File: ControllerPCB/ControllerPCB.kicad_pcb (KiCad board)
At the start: 2 copper layers, 48 parts, among them U2 STM32F439ZITx, Y2 WE-XTAL_CFPX-218

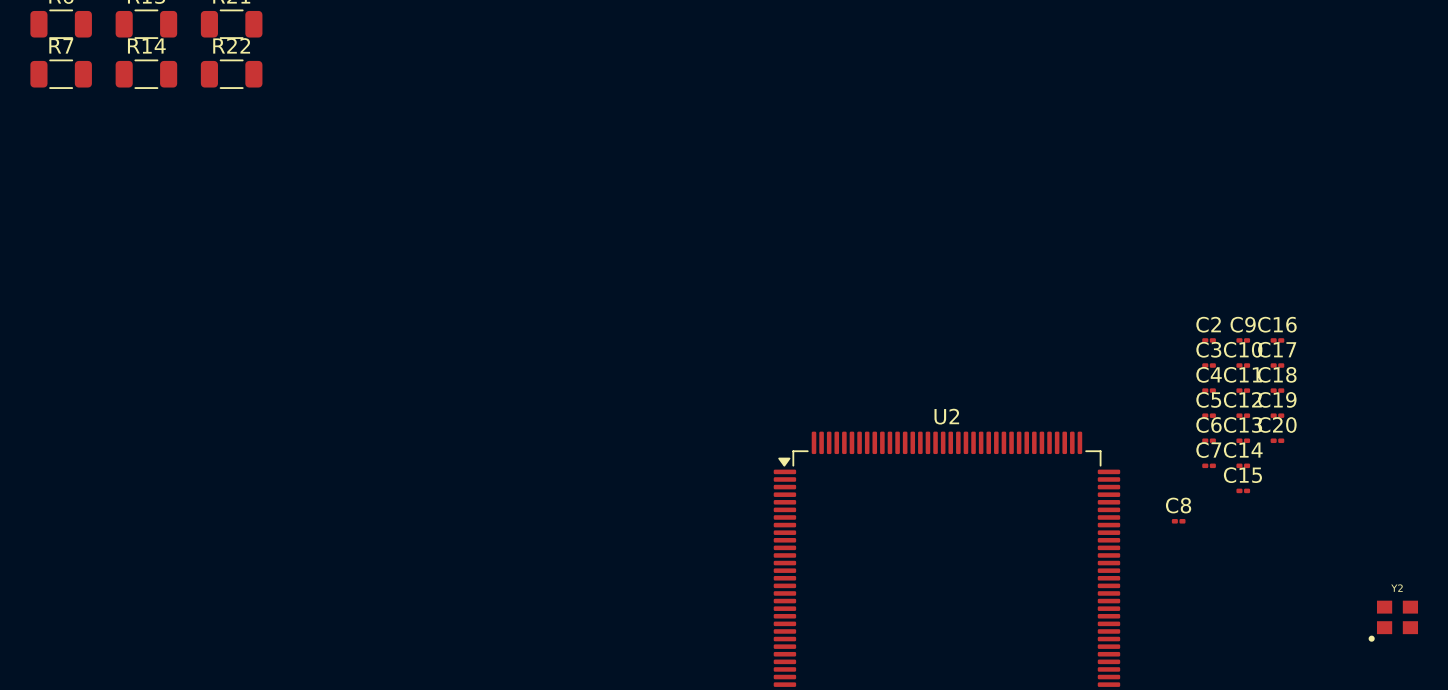
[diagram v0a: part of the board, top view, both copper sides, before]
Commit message: Added footprints to the resistors and capacitors and values of Crystall Oscillator capacitors.
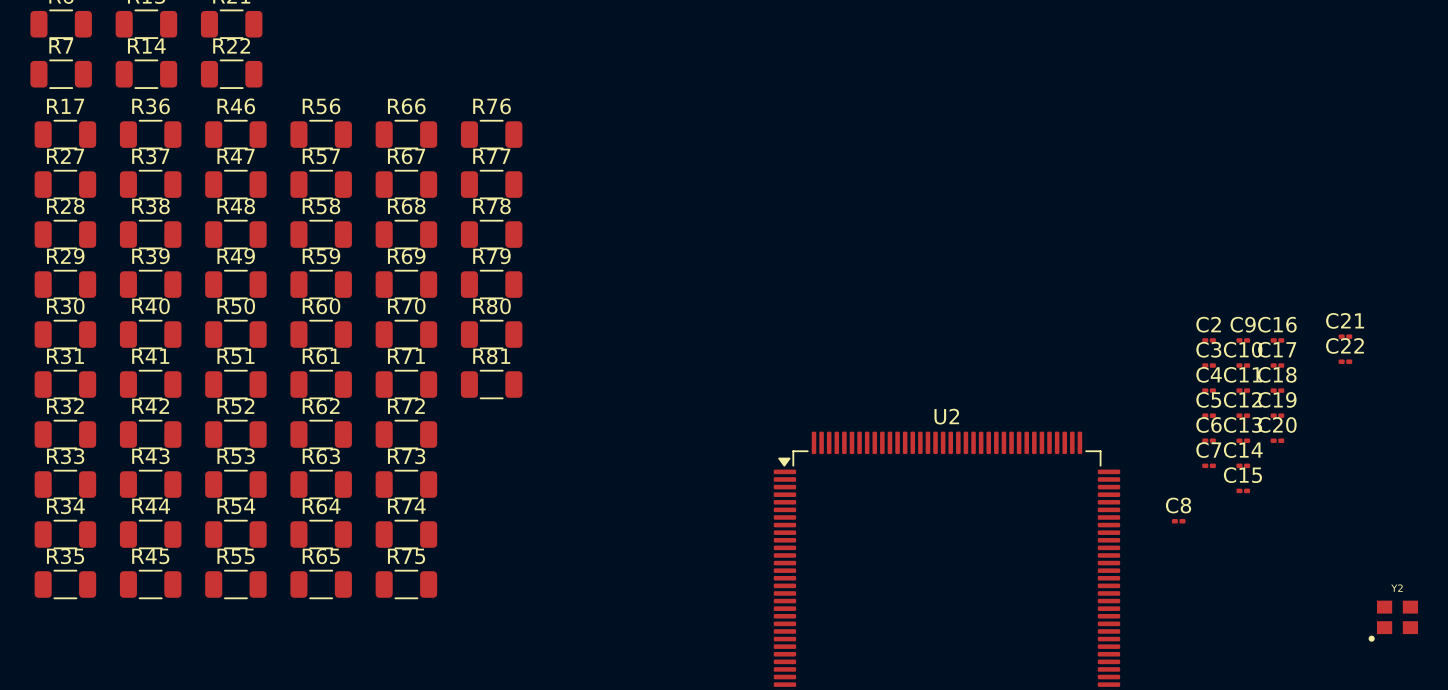
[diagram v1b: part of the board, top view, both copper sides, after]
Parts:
- added C21: 10p, Capacitor_SMD:C_01005_0402Metric, F.Cu at (170.7, 78.3)
- added C22: 10p, Capacitor_SMD:C_01005_0402Metric, F.Cu at (170.7, 80.0)
- added R17: 10k, Resistor_SMD:R_1206_3216Metric, F.Cu at (86.5, 65.0)
- added R27: 10k, Resistor_SMD:R_1206_3216Metric, F.Cu at (86.5, 68.3)
- added R28: 10k, Resistor_SMD:R_1206_3216Metric, F.Cu at (86.5, 71.6)
- added R29: 10k, Resistor_SMD:R_1206_3216Metric, F.Cu at (86.5, 74.9)
- added R30: 10k, Resistor_SMD:R_1206_3216Metric, F.Cu at (86.5, 78.2)
- added R31: 10k, Resistor_SMD:R_1206_3216Metric, F.Cu at (86.5, 81.5)
- added R32: 10k, Resistor_SMD:R_1206_3216Metric, F.Cu at (86.5, 84.8)
- added R33: 10k, Resistor_SMD:R_1206_3216Metric, F.Cu at (86.5, 88.1)
- added R34: 10k, Resistor_SMD:R_1206_3216Metric, F.Cu at (86.5, 91.4)
- added R35: 10k, Resistor_SMD:R_1206_3216Metric, F.Cu at (86.5, 94.7)
- added R36: 10k, Resistor_SMD:R_1206_3216Metric, F.Cu at (92.1, 65.0)
- added R37: 10k, Resistor_SMD:R_1206_3216Metric, F.Cu at (92.1, 68.3)
- added R38: 10k, Resistor_SMD:R_1206_3216Metric, F.Cu at (92.1, 71.6)
- added R39: 10k, Resistor_SMD:R_1206_3216Metric, F.Cu at (92.1, 74.9)
- added R40: 10k, Resistor_SMD:R_1206_3216Metric, F.Cu at (92.1, 78.2)
- added R41: 10k, Resistor_SMD:R_1206_3216Metric, F.Cu at (92.1, 81.5)
- added R42: 10k, Resistor_SMD:R_1206_3216Metric, F.Cu at (92.1, 84.8)
- added R43: 10k, Resistor_SMD:R_1206_3216Metric, F.Cu at (92.1, 88.1)
- added R44: 10k, Resistor_SMD:R_1206_3216Metric, F.Cu at (92.1, 91.4)
- added R45: 10k, Resistor_SMD:R_1206_3216Metric, F.Cu at (92.1, 94.7)
- added R46: 10k, Resistor_SMD:R_1206_3216Metric, F.Cu at (97.7, 65.0)
- added R47: 10k, Resistor_SMD:R_1206_3216Metric, F.Cu at (97.7, 68.3)
- added R48: 10k, Resistor_SMD:R_1206_3216Metric, F.Cu at (97.7, 71.6)
- added R49: 10k, Resistor_SMD:R_1206_3216Metric, F.Cu at (97.7, 74.9)
- added R50: 10k, Resistor_SMD:R_1206_3216Metric, F.Cu at (97.7, 78.2)
- added R51: 10k, Resistor_SMD:R_1206_3216Metric, F.Cu at (97.7, 81.5)
- added R52: 10k, Resistor_SMD:R_1206_3216Metric, F.Cu at (97.7, 84.8)
- added R53: 10k, Resistor_SMD:R_1206_3216Metric, F.Cu at (97.7, 88.1)
- added R54: 10k, Resistor_SMD:R_1206_3216Metric, F.Cu at (97.7, 91.4)
- added R55: 10k, Resistor_SMD:R_1206_3216Metric, F.Cu at (97.7, 94.7)
- added R56: 10k, Resistor_SMD:R_1206_3216Metric, F.Cu at (103.3, 65.0)
- added R57: 10k, Resistor_SMD:R_1206_3216Metric, F.Cu at (103.3, 68.3)
- added R58: 10k, Resistor_SMD:R_1206_3216Metric, F.Cu at (103.3, 71.6)
- added R59: 10k, Resistor_SMD:R_1206_3216Metric, F.Cu at (103.3, 74.9)
- added R60: 10k, Resistor_SMD:R_1206_3216Metric, F.Cu at (103.3, 78.2)
- added R61: 10k, Resistor_SMD:R_1206_3216Metric, F.Cu at (103.3, 81.5)
- added R62: 10k, Resistor_SMD:R_1206_3216Metric, F.Cu at (103.3, 84.8)
- added R63: 10k, Resistor_SMD:R_1206_3216Metric, F.Cu at (103.3, 88.1)
- added R64: 10k, Resistor_SMD:R_1206_3216Metric, F.Cu at (103.3, 91.4)
- added R65: 10k, Resistor_SMD:R_1206_3216Metric, F.Cu at (103.3, 94.7)
- added R66: 10k, Resistor_SMD:R_1206_3216Metric, F.Cu at (108.9, 65.0)
- added R67: 10k, Resistor_SMD:R_1206_3216Metric, F.Cu at (108.9, 68.3)
- added R68: 10k, Resistor_SMD:R_1206_3216Metric, F.Cu at (108.9, 71.6)
- added R69: 10k, Resistor_SMD:R_1206_3216Metric, F.Cu at (108.9, 74.9)
- added R70: 10k, Resistor_SMD:R_1206_3216Metric, F.Cu at (108.9, 78.2)
- added R71: 10k, Resistor_SMD:R_1206_3216Metric, F.Cu at (108.9, 81.5)
- added R72: 10k, Resistor_SMD:R_1206_3216Metric, F.Cu at (108.9, 84.8)
- added R73: 10k, Resistor_SMD:R_1206_3216Metric, F.Cu at (108.9, 88.1)
- added R74: 10k, Resistor_SMD:R_1206_3216Metric, F.Cu at (108.9, 91.4)
- added R75: 10k, Resistor_SMD:R_1206_3216Metric, F.Cu at (108.9, 94.7)
- added R76: 10k, Resistor_SMD:R_1206_3216Metric, F.Cu at (114.5, 65.0)
- added R77: 10k, Resistor_SMD:R_1206_3216Metric, F.Cu at (114.5, 68.3)
- added R78: 10k, Resistor_SMD:R_1206_3216Metric, F.Cu at (114.5, 71.6)
- added R79: 10k, Resistor_SMD:R_1206_3216Metric, F.Cu at (114.5, 74.9)
- added R80: 10k, Resistor_SMD:R_1206_3216Metric, F.Cu at (114.5, 78.2)
- added R81: 10k, Resistor_SMD:R_1206_3216Metric, F.Cu at (114.5, 81.5)

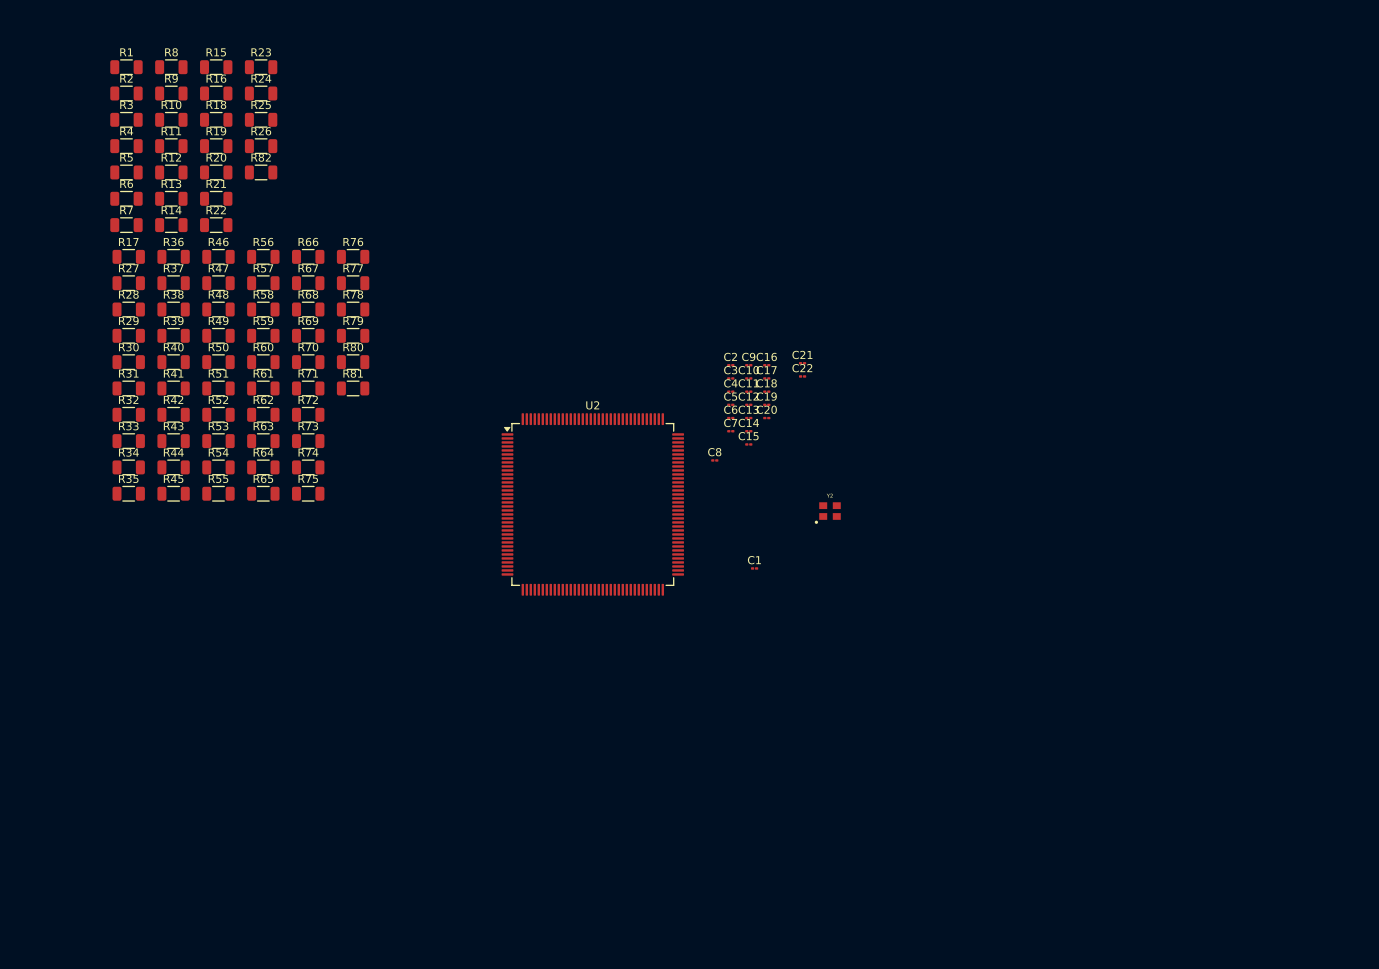
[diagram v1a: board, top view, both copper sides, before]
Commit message: Began the PCB. Placed the decoupling caps, usb micro b conn and others. Adding footprints for components as well.
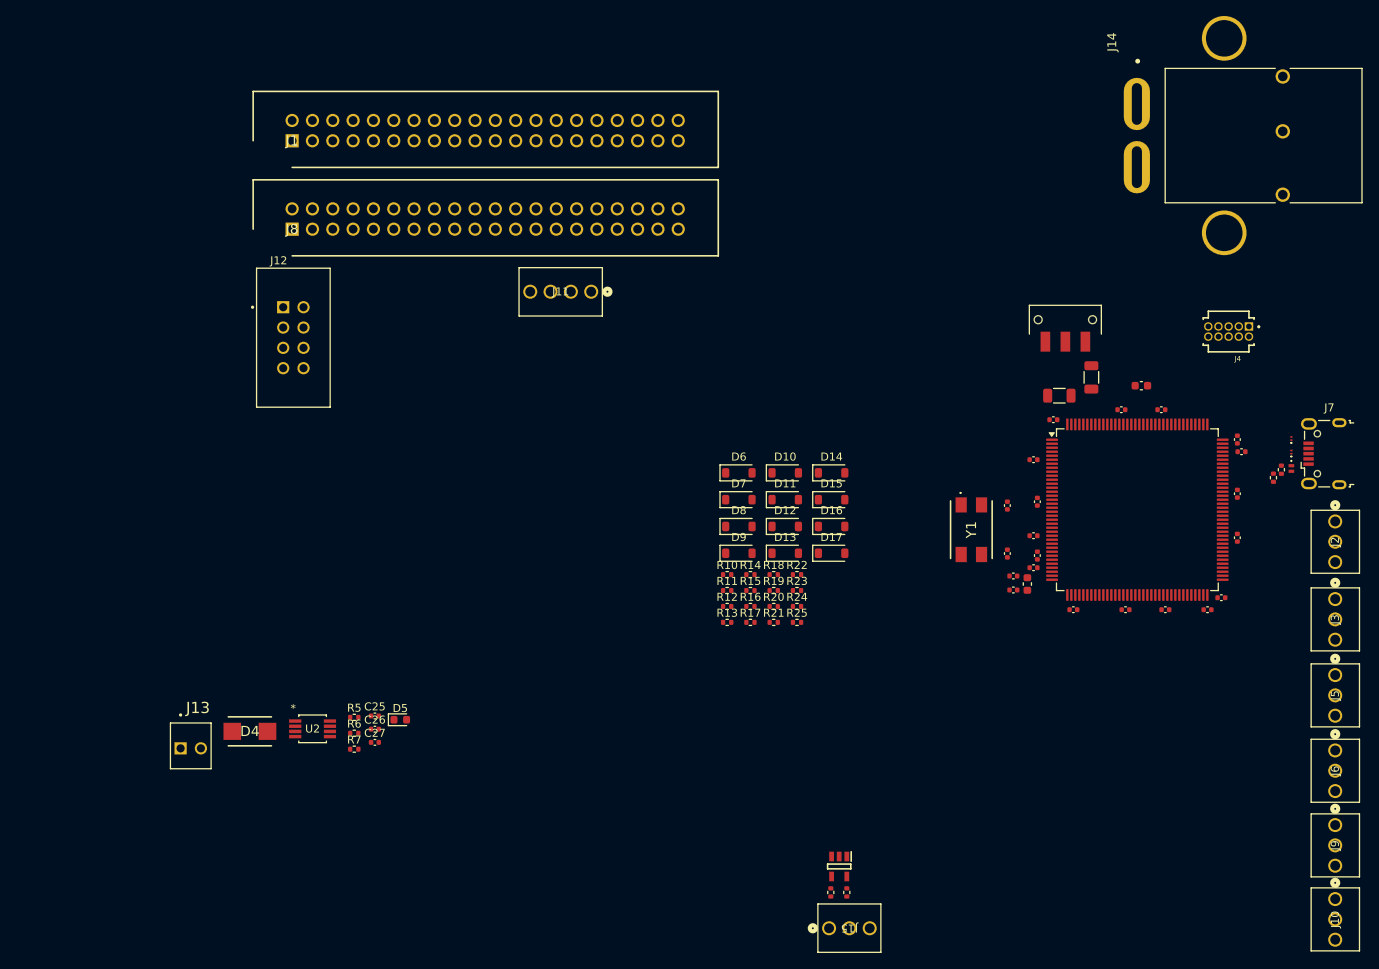
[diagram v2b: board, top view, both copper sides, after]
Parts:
- removed the C19 at (166.2, 83.5)
- removed C20: 1u, Capacitor_SMD:C_01005_0402Metric
- removed the R2 at (86.2, 44.6)
- removed R26, R27, R28, R29, R30, R31, R32, R33, R34, R35, R36, R37, R38, R39, R40, R41, R42, R43, R44, R45, R46, R47, R48, R49, R50, R51, R52, R53, R54, R55, R56, R57, R58, R59, R60, R61, R62, R63, R64, R65, R66, R67, R68, R69, R70, R71, R72, R73, R74, R75, R76, R77, R78, R79, R80, R81: 10k, Resistor_SMD:R_1206_3216Metric
- removed Y2: WE-XTAL_CFPX-218, crysoscill:WE-SPXO_IQXO-791
- added C14: 2.2u, Capacitor_SMD:C_0402_1005Metric, F.Cu at (221.3, 109.2)
- added C17: 2.2u, Capacitor_SMD:C_0402_1005Metric, F.Cu at (225.6, 89.4)
- added C25: 1u, Capacitor_SMD:C_0402_1005Metric, F.Cu at (117.3, 122.4)
- added C26: 100p, Capacitor_SMD:C_0402_1005Metric, F.Cu at (117.3, 124.1)
- added C27: 1u, Capacitor_SMD:C_0402_1005Metric, F.Cu at (117.3, 125.7)
- added D1: D+_TVS, PESD3V6Z1BCSFYL:PMEG3005AESFYL, F.Cu at (231.8, 87.9)
- added D10: MBR0520LT, Diode_SMD:D_SOD-123, F.Cu at (168.6, 92.0)
- added D11: MBR0520LT, Diode_SMD:D_SOD-123, F.Cu at (168.6, 95.4)
- added D12: MBR0520LT, Diode_SMD:D_SOD-123, F.Cu at (168.6, 98.8)
- added D13: MBR0520LT, Diode_SMD:D_SOD-123, F.Cu at (168.6, 102.1)
- added D14: MBR0520LT, Diode_SMD:D_SOD-123, F.Cu at (174.3, 92.0)
- added D15: MBR0520LT, Diode_SMD:D_SOD-123, F.Cu at (174.3, 95.4)
- added D16: MBR0520LT, Diode_SMD:D_SOD-123, F.Cu at (174.3, 98.8)
- added D17: MBR0520LT, Diode_SMD:D_SOD-123, F.Cu at (174.3, 102.1)
- added D2: VBUS_TVS, PESD5V5C1BLYL:PESD5V5C1BLYL, F.Cu at (231.8, 91.5)
- added D3: D-_TVS, PESD3V6Z1BCSFYL:PMEG3005AESFYL, F.Cu at (231.8, 89.6)
- added D4: TVS_Bat, TPSMB10CA:DIONM5436X244N, F.Cu at (101.6, 124.4)
- added D5: GRN, LED_SMD:LED_0603_1608Metric, F.Cu at (120.4, 122.9)
- added D6: MBR0520LT, Diode_SMD:D_SOD-123, F.Cu at (162.8, 92.0)
- added D7: MBR0520LT, Diode_SMD:D_SOD-123, F.Cu at (162.8, 95.4)
- added D8: MBR0520LT, Diode_SMD:D_SOD-123, F.Cu at (162.8, 98.8)
- added D9: MBR0520LT, Diode_SMD:D_SOD-123, F.Cu at (162.8, 102.1)
- added FB1: 120R, Inductor_SMD:L_0603_1608Metric, F.Cu at (198.8, 105.9)
- added J1: 2x20 Conn_1, 75869-107LF:SHDR40W62P254_2X20_5801X920X957P, F.Cu at (106.9, 50.5)
- added J10: Conn_01x03_Pin, 22292031:CONN_AE-6410-03A_MOL, F.Cu at (237.3, 145.3)
- added J11: 1x4 String Output Conn, 22292041:CONN_AE-6410-04A_MOL, F.Cu at (144.3, 69.4)
- added J12: 2x4 Pickup Conn, 75869_332LF:AMPHENOL_75869-332LF, F.Cu at (107.1, 75.2)
- added J13: 9V Humbucker OUT, 3_641126_2:TE_3-641126-2, F.Cu at (94.2, 126.5)
- added J14: 9V IN, PowerConnector:APP_ASMPR45-1X2-RK, F.Cu at (212.5, 45.9)
- added J15: MIDI Out Conn, 22292031:CONN_AE-6410-03A_MOL, F.Cu at (174.0, 149.0)
- added J2: Conn_01x03_Pin, 22292031:CONN_AE-6410-03A_MOL, F.Cu at (237.3, 98.1)
- added J3: Conn_01x03_Pin, 22292031:CONN_AE-6410-03A_MOL, F.Cu at (237.3, 107.8)
- added J4: 10-pin Debug Conn, FTSH_105_01_F_D_K:SAMTEC_FTSH-105-01-F-D-K, F.Cu at (224.0, 74.4)
- added J5: Conn_01x03_Pin, 22292031:CONN_AE-6410-03A_MOL, F.Cu at (237.3, 117.3)
- added J6: Conn_01x03_Pin, 22292031:CONN_AE-6410-03A_MOL, F.Cu at (237.3, 126.7)
- added J7: USB_B_Micro, Connector_USB:USB_Micro-B_Wuerth_629105150521, F.Cu at (235.9, 89.7)
- added J8: 2x20 Conn_2, 75869-107LF:SHDR40W62P254_2X20_5801X920X957P, F.Cu at (106.9, 61.6)
- added J9: Conn_01x03_Pin, 22292031:CONN_AE-6410-03A_MOL, F.Cu at (237.3, 136.1)
- added SW1: SW_SPDT, JS102011SAQN:SW_JS102011SAQN, F.Cu at (203.6, 72.9)
- added U2: ADP3336ARMZ, ADP3336ARMZ_REEL7:RM_8_ADI, F.Cu at (109.5, 124.0)
- added U3: 74LVC1G17, SN74LVC1G17DBVR:SOT95P280X145-5N, F.Cu at (175.3, 141.2)
- added Y1: 8MHz, 830059082:830059082, F.Cu at (191.8, 99.2)
- C1: renamed from C14; footprint Capacitor_SMD:C_01005_0402Metric -> Capacitor_SMD:C_0603_1608Metric
- C10: renamed from C6; footprint Capacitor_SMD:C_01005_0402Metric -> Capacitor_SMD:C_0402_1005Metric
- C11: renamed from C7; footprint Capacitor_SMD:C_01005_0402Metric -> Capacitor_SMD:C_0402_1005Metric
- C12: renamed from C21; footprint Capacitor_SMD:C_01005_0402Metric -> Capacitor_SMD:C_0402_1005Metric
- C13: renamed from C8; footprint Capacitor_SMD:C_01005_0402Metric -> Capacitor_SMD:C_0402_1005Metric
- C15: renamed from C3; footprint Capacitor_SMD:C_01005_0402Metric -> Capacitor_SMD:C_0402_1005Metric
- C16: renamed from C4; footprint Capacitor_SMD:C_01005_0402Metric -> Capacitor_SMD:C_0402_1005Metric
- C18: renamed from C2; footprint Capacitor_SMD:C_01005_0402Metric -> Capacitor_SMD:C_0402_1005Metric
- C19: renamed from C1; footprint Capacitor_SMD:C_01005_0402Metric -> Capacitor_SMD:C_0402_1005Metric
- C2: renamed from C13; footprint Capacitor_SMD:C_01005_0402Metric -> Capacitor_SMD:C_0402_1005Metric
- C22: renamed from C15; footprint Capacitor_SMD:C_01005_0402Metric -> Capacitor_SMD:C_0402_1005Metric
- C23: renamed from C16; footprint Capacitor_SMD:C_01005_0402Metric -> Capacitor_SMD:C_0402_1005Metric
- C24: renamed from C17; footprint Capacitor_SMD:C_01005_0402Metric -> Capacitor_SMD:C_0402_1005Metric
- C3: renamed from C9; footprint Capacitor_SMD:C_01005_0402Metric -> Capacitor_SMD:C_0402_1005Metric
- C4: renamed from C10; footprint Capacitor_SMD:C_01005_0402Metric -> Capacitor_SMD:C_0402_1005Metric
- C5: renamed from C11; footprint Capacitor_SMD:C_01005_0402Metric -> Capacitor_SMD:C_0402_1005Metric
- C6: renamed from C18; footprint Capacitor_SMD:C_01005_0402Metric -> Capacitor_SMD:C_0402_1005Metric
- C7: renamed from C12; footprint Capacitor_SMD:C_01005_0402Metric -> Capacitor_SMD:C_0402_1005Metric
- C8: renamed from C22; footprint Capacitor_SMD:C_01005_0402Metric -> Capacitor_SMD:C_0402_1005Metric
- C9: renamed from C5; footprint Capacitor_SMD:C_01005_0402Metric -> Capacitor_SMD:C_0402_1005Metric
- R10, R11, R18, R19: value 10k -> 5k; footprint Resistor_SMD:R_1206_3216Metric -> Resistor_SMD:R_0402_1005Metric
- R12, R14, R20, R22, R7: value 10k -> 1k; footprint Resistor_SMD:R_1206_3216Metric -> Resistor_SMD:R_0402_1005Metric
- R13, R15, R21, R23: footprint Resistor_SMD:R_1206_3216Metric -> Resistor_SMD:R_0402_1005Metric
- R16, R17, R24, R25: value 10k -> 2k; footprint Resistor_SMD:R_1206_3216Metric -> Resistor_SMD:R_0402_1005Metric
- R3: value 10k -> 33k; footprint Resistor_SMD:R_1206_3216Metric -> Resistor_SMD:R_0402_1005Metric
- R4: value 10k -> 82k; footprint Resistor_SMD:R_1206_3216Metric -> Resistor_SMD:R_0402_1005Metric
- R5: value 10k -> 140k; footprint Resistor_SMD:R_1206_3216Metric -> Resistor_SMD:R_0402_1005Metric
- R6: value 10k -> 78.7k; footprint Resistor_SMD:R_1206_3216Metric -> Resistor_SMD:R_0402_1005Metric
- R8: value 10k -> 33R; footprint Resistor_SMD:R_1206_3216Metric -> Resistor_SMD:R_0402_1005Metric
- R9: value 10k -> 10R; footprint Resistor_SMD:R_1206_3216Metric -> Resistor_SMD:R_0402_1005Metric
- U1: renamed from U2; value STM32F439ZITx -> STM32F439ZIT6
- moved R3 150.8 mm to (230.6, 91.7), turned to -90 degrees
- moved R4 149.2 mm to (229.6, 92.7), turned to -90 degrees
- moved R8 133.3 mm to (176.2, 144.5), turned to -90 degrees
- moved R9 129.5 mm to (174.2, 144.5), turned to -90 degrees
- moved R2 126.7 mm to (206.8, 80.1), turned to -90 degrees
- moved R1 103.6 mm to (202.8, 82.4)
- moved R23 93.6 mm to (170.0, 106.8)
- moved R15 93.5 mm to (164.2, 106.8)
- moved R24 92.7 mm to (170.0, 108.8)
- moved R16 92.6 mm to (164.2, 108.8)
- moved R25 91.8 mm to (170.0, 110.7)
- moved R17 90.2 mm to (164.2, 110.7)
- moved R18 89.9 mm to (167.1, 104.8)
- moved R10 89.8 mm to (161.3, 104.8)
- moved R19 89.1 mm to (167.1, 106.8)
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- renumbered R82 to R1, R1 to R2
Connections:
- net /NRST renamed NRST
- C1 pad 1: VREF+ -> +3.3V
- C10 pad 1: VREF+ -> +3.3V
- C11 pad 1: VREF+ -> +3.3V
- C12 pad 1: Net-(U2-PH0) -> /HSE_OUT
- C13 pad 1: VREF+ -> +3.3V
- C15 pad 1: VREF+ -> +3.3V
- C16 pad 1: VREF+ -> +3.3V
- C18 pad 1: VREF+ -> +3.3V
- C19 pad 1: VREF+ -> +3.3V
- C2 pad 1: VREF+ -> +3.3V
- C22 pad 1: VREF+ -> +3.3VA
- C23 pad 1: VREF+ -> +3.3VA
- C24 pad 1: VREF+ -> +3.3V
- C3 pad 1: VREF+ -> +3.3V
- C4 pad 1: VREF+ -> +3.3V
- C5 pad 1: VREF+ -> +3.3V
- C7 pad 1: VREF+ -> +3.3V
- C8 pad 1: Net-(U2-PH1) -> /HSE_IN
- C9 pad 1: VREF+ -> +3.3V
- R1 pad 1: VREF+ -> +3.3V
- R10 pad 1: Net-(U2-PB8) -> ADC_String_1
- R11 pad 1: Net-(U2-PB9) -> ADC_String_2
- R12 pad 1: Net-(U2-PB10) -> +3.3V
- R12 pad 2: Net-(J1-Pin_a11) -> Net-(R12-Pad2)
- R13 pad 1: Net-(U2-PB11) -> Net-(R12-Pad2)
- R13 pad 2: Net-(J1-Pin_a12) -> GND
- R14 pad 1: Net-(U2-PB12) -> +3.3V
- R14 pad 2: Net-(J1-Pin_a13) -> Net-(R14-Pad2)
- R15 pad 1: Net-(U2-PB13) -> Net-(R14-Pad2)
- R15 pad 2: Net-(J1-Pin_a14) -> GND
- R16 pad 1: Net-(U2-PB14) -> Net-(R12-Pad2)
- R17 pad 1: Net-(U2-PB15) -> Net-(R14-Pad2)
- R18 pad 1: Net-(U2-PC0) -> ADC_String_3
- R19 pad 1: Net-(U2-PC1) -> ADC_String_4
- R20 pad 1: Net-(U2-PC2) -> +3.3V
- R20 pad 2: Net-(J1-Pin_a19) -> Net-(R20-Pad2)
- R21 pad 1: Net-(U2-PC3) -> Net-(R20-Pad2)
- R21 pad 2: Net-(J1-Pin_a20) -> GND
- R22 pad 1: Net-(U2-PC4) -> +3.3V
- R22 pad 2: Net-(J1-Pin_a21) -> Net-(R22-Pad2)
- R23 pad 1: Net-(U2-PC5) -> Net-(R22-Pad2)
- R23 pad 2: Net-(J1-Pin_a22) -> GND
- R24 pad 1: Net-(U2-PC6) -> Net-(R20-Pad2)
- R25 pad 1: Net-(U2-PC7) -> Net-(R22-Pad2)
- R3 pad 1: Net-(U2-PB1) -> /VBUS_TVS
- R3 pad 2: Net-(J1-Pin_a2) -> VBUS_Sense
- R4 pad 1: Net-(U2-PB2) -> VBUS_Sense
- R4 pad 2: Net-(J1-Pin_a3) -> GND
- R5 pad 1: Net-(U2-PB3) -> +3.3V
- R5 pad 2: Net-(J1-Pin_a4) -> Net-(U2-FB)
- R6 pad 1: Net-(U2-PB4) -> Net-(U2-FB)
- R6 pad 2: Net-(J1-Pin_a5) -> GND
- R7 pad 1: Net-(U2-PB5) -> Net-(D5-K)
- R7 pad 2: Net-(J1-Pin_a6) -> GND
- R8 pad 1: Net-(U2-PB6) -> +3.3V
- R8 pad 2: Net-(J1-Pin_a7) -> /MIDI OUT/+3.3V_MIDI_OUT
- R9 pad 1: Net-(U2-PB7) -> /MIDI OUT/TX_BUF_OUT
- R9 pad 2: Net-(J1-Pin_a8) -> /MIDI OUT/TX_MIDI_OUT
- U1 pad 1: unconnected-(U2-PE2-Pad1) -> input_40
- U1 pad 10: PF0 -> input_54
- U1 pad 100: unconnected-(U2-PA8-Pad100) -> input_1
- U1 pad 101: unconnected-(U2-PA9-Pad101) -> VBUS_Sense
- U1 pad 102: unconnected-(U2-PA10-Pad102) -> input_2
- U1 pad 103: unconnected-(U2-PA11-Pad103) -> D-
- U1 pad 104: unconnected-(U2-PA12-Pad104) -> D+
- U1 pad 105: unconnected-(U2-PA13-Pad105) -> SWDIO
- U1 pad 106: unconnected-(U2-VCAP_2-Pad106) -> /VCAP_2
- U1 pad 108: VREF+ -> +3.3V
- U1 pad 109: unconnected-(U2-PA14-Pad109) -> SWDCLK
- U1 pad 11: PF1 -> input_55
- U1 pad 110: unconnected-(U2-PA15-Pad110) -> input_3
- U1 pad 111: Net-(U2-PC10) -> input_19
- U1 pad 112: Net-(U2-PC11) -> input_20
- U1 pad 113: Net-(U2-PC12) -> input_21
- U1 pad 114: Net-(U2-PD0) -> input_25
- U1 pad 115: Net-(U2-PD1) -> input_26
- U1 pad 116: Net-(U2-PD2) -> input_27
- U1 pad 117: Net-(U2-PD3) -> input_28
- U1 pad 118: Net-(U2-PD4) -> input_29
- U1 pad 119: Net-(U2-PD5) -> input_30
- U1 pad 12: PF2 -> input_56
- U1 pad 121: VREF+ -> +3.3V
- U1 pad 122: Net-(U2-PD6) -> input_31
- U1 pad 123: Net-(U2-PD7) -> input_32
- U1 pad 124: PG9 -> input_79
- U1 pad 125: PG10 -> String_1_out
- U1 pad 126: PG11 -> String_2_out
- U1 pad 127: PG12 -> String_3_out
- U1 pad 128: PG13 -> String_4_out
- U1 pad 129: PG14 -> input_80
- U1 pad 13: PF3 -> input_57
- U1 pad 131: VREF+ -> +3.3V
- U1 pad 132: PG15 -> unconnected-(U1-PG15-Pad132)
- U1 pad 133: Net-(U2-PB3) -> SWO
- U1 pad 134: Net-(U2-PB4) -> unconnected-(U1-PB4-Pad134)
- U1 pad 135: Net-(U2-PB5) -> unconnected-(U1-PB5-Pad135)
- U1 pad 136: Net-(U2-PB6) -> unconnected-(U1-PB6-Pad136)
- U1 pad 137: Net-(U2-PB7) -> unconnected-(U1-PB7-Pad137)
- U1 pad 139: Net-(U2-PB8) -> unconnected-(U1-PB8-Pad139)
- U1 pad 14: PF4 -> input_58
- U1 pad 140: Net-(U2-PB9) -> unconnected-(U1-PB9-Pad140)
- U1 pad 144: VREF+ -> +3.3V
- U1 pad 15: PF5 -> input_59
- U1 pad 17: VREF+ -> +3.3V
- U1 pad 18: PF6 -> input_60
- U1 pad 19: PF7 -> input_61
- U1 pad 2: unconnected-(U2-PE3-Pad2) -> input_41
- U1 pad 20: PF8 -> input_62
- U1 pad 21: PF9 -> input_63
- U1 pad 22: PF10 -> input_64
- U1 pad 23: Net-(U2-PH0) -> /HSE_IN
- U1 pad 24: Net-(U2-PH1) -> /HSE_OUT
- U1 pad 26: Net-(U2-PC0) -> unconnected-(U1-PC0-Pad26)
- U1 pad 27: Net-(U2-PC1) -> input_10
- U1 pad 28: Net-(U2-PC2) -> input_11
- U1 pad 29: Net-(U2-PC3) -> input_12
- U1 pad 3: unconnected-(U2-PE4-Pad3) -> input_42
- U1 pad 30: VREF+ -> +3.3V
- U1 pad 32: VREF+ -> +3.3VA
- U1 pad 33: VREF+ -> +3.3VA
- U1 pad 34: unconnected-(U2-PA0-Pad34) -> ADC_String_1_F
- U1 pad 35: unconnected-(U2-PA1-Pad35) -> ADC_String_2_F
- U1 pad 36: unconnected-(U2-PA2-Pad36) -> ADC_String_3_F
- U1 pad 37: unconnected-(U2-PA3-Pad37) -> ADC_String_4_F
- U1 pad 39: VREF+ -> +3.3V
- U1 pad 4: unconnected-(U2-PE5-Pad4) -> input_43
- U1 pad 40: unconnected-(U2-PA4-Pad40) -> ADC_Octave
- U1 pad 41: unconnected-(U2-PA5-Pad41) -> ADC_Mod
- U1 pad 42: unconnected-(U2-PA6-Pad42) -> ADC_Bend
- U1 pad 43: unconnected-(U2-PA7-Pad43) -> ADC_MIDI_Ch
- U1 pad 44: Net-(U2-PC4) -> input_13
- U1 pad 45: Net-(U2-PC5) -> input_14
- U1 pad 46: Net-(U2-PB0) -> ADC_Thresh
- U1 pad 47: Net-(U2-PB1) -> ADC_Extra
- U1 pad 48: Net-(U2-PB2) -> unconnected-(U1-PB2-Pad48)
- U1 pad 49: PF11 -> input_65
- U1 pad 5: unconnected-(U2-PE6-Pad5) -> input_44
- U1 pad 50: PF12 -> input_66
- U1 pad 52: VREF+ -> +3.3V
- U1 pad 53: PF13 -> input_67
- U1 pad 54: PF14 -> input_68
- U1 pad 55: PF15 -> input_69
- U1 pad 56: PG0 -> input_70
- U1 pad 57: PG1 -> input_71
- U1 pad 58: unconnected-(U2-PE7-Pad58) -> input_45
- U1 pad 59: String1 -> input_46
- U1 pad 6: VREF+ -> +3.3V
- U1 pad 60: String2 -> input_47
- U1 pad 62: VREF+ -> +3.3V
- U1 pad 63: String3 -> input_48
- U1 pad 64: String4 -> input_49
- U1 pad 65: unconnected-(U2-PE12-Pad65) -> input_50
- U1 pad 66: unconnected-(U2-PE13-Pad66) -> input_51
- U1 pad 67: unconnected-(U2-PE14-Pad67) -> input_52
- U1 pad 68: unconnected-(U2-PE15-Pad68) -> input_53
- U1 pad 69: Net-(U2-PB10) -> input_4
- U1 pad 7: Net-(U2-PC13) -> input_22
- U1 pad 70: Net-(U2-PB11) -> input_5
- U1 pad 71: unconnected-(U2-VCAP_1-Pad71) -> /VCAP_1
- U1 pad 72: VREF+ -> +3.3V
- U1 pad 73: Net-(U2-PB12) -> input_6
- U1 pad 74: Net-(U2-PB13) -> input_7
- U1 pad 75: Net-(U2-PB14) -> input_8
- U1 pad 76: Net-(U2-PB15) -> input_9
- U1 pad 77: Net-(U2-PD8) -> UART_TX
- U1 pad 78: Net-(U2-PD9) -> input_33
- U1 pad 79: Net-(U2-PD10) -> input_34
- U1 pad 8: Net-(U2-PC14) -> input_23
- U1 pad 80: Net-(U2-PD11) -> input_35
- U1 pad 81: Net-(U2-PD12) -> input_36
- U1 pad 82: Net-(U2-PD13) -> input_37
- U1 pad 84: VREF+ -> +3.3V
- U1 pad 85: Net-(U2-PD14) -> input_38
- U1 pad 86: Net-(U2-PD15) -> input_39
- U1 pad 87: PG2 -> input_72
- U1 pad 88: PG3 -> input_73
- U1 pad 89: PG4 -> input_74
- U1 pad 9: Net-(U2-PC15) -> input_24
- U1 pad 90: PG5 -> input_75
- U1 pad 91: PG6 -> input_76
- U1 pad 92: PG7 -> input_77
- U1 pad 93: PG8 -> input_78
- U1 pad 95: VREF+ -> +3.3V
- U1 pad 96: Net-(U2-PC6) -> input_15
- U1 pad 97: Net-(U2-PC7) -> input_16
- U1 pad 98: Net-(U2-PC8) -> input_17
- U1 pad 99: Net-(U2-PC9) -> input_18
